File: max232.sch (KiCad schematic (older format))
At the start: 10 parts, among them J1 DB9, J2 DB9, P1 CONN_4, P2 CONN_4, U1 MAX232

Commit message: Version for iStudio.
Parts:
- removed J2: DB9, symbol DB9
- removed P1, P2: CONN_4, symbol CONN_4
- added P1: CONN_6, symbol CONN_6
- added P2, P3, P4, P5: CONN_1, symbol CONN_1
- added Q1, Q2: MOSFET_N, symbol MOSFET_N
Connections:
- net labels added: RD, RD_, TD, TD_
- wire segments 47 -> 59
- no-connect marks 12 -> 4

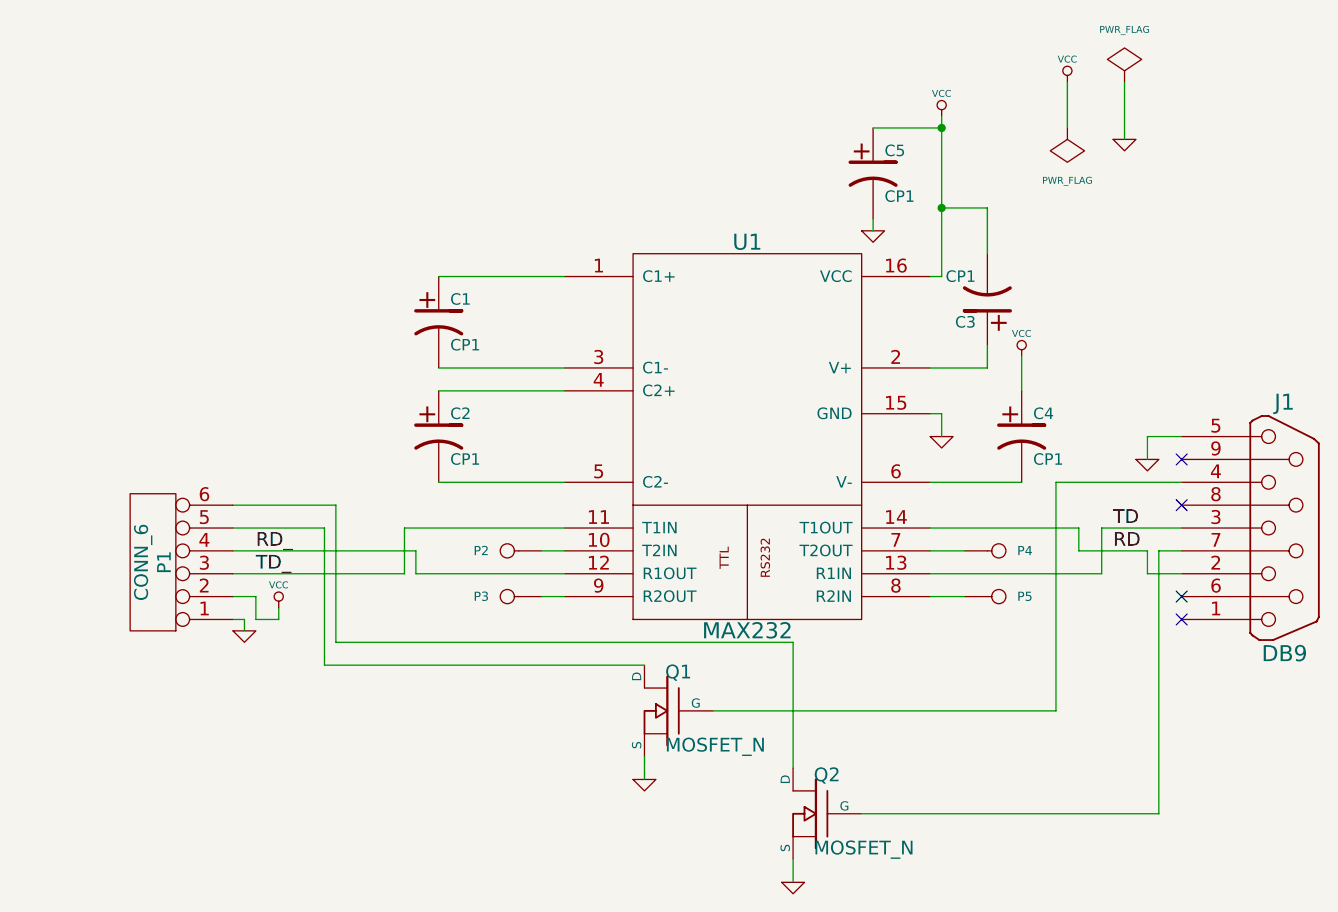
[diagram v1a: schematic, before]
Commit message: Fixed schemantick.
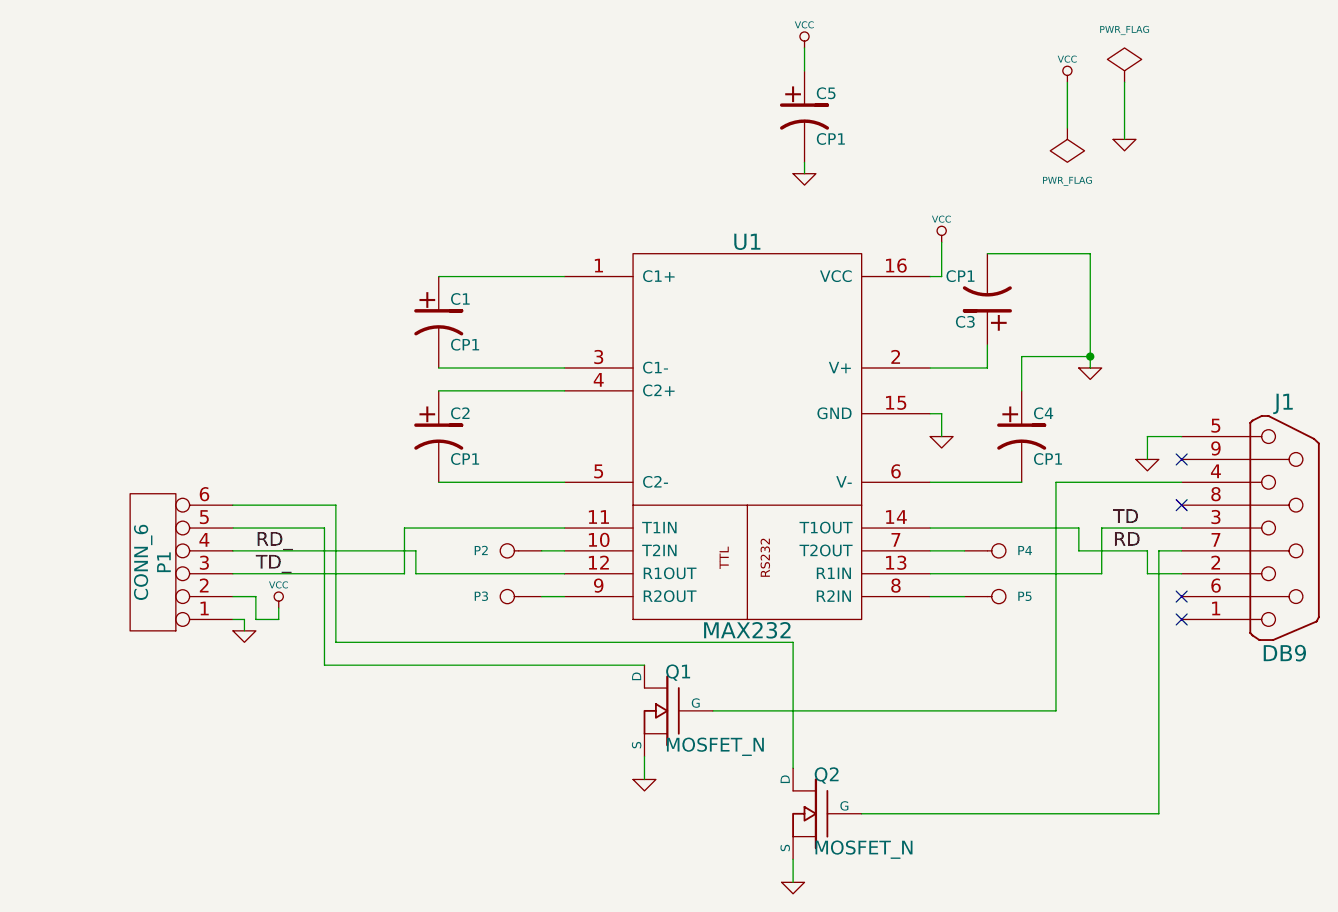
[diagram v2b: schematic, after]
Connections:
- net GND: now also C3.2, C4.1
- net VCC: no longer C3.2, C4.1
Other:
- moved on the sheet: C5
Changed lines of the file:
@@
-EESchema Schematic File Version 2  date Чт. 15 авг. 2013 22:17:01
+EESchema Schematic File Version 2  date Чт 05 сен 2013 11:55:04
 LIBS:power
 LIBS:device
@@
 Sheet 1 1
 Title ""
-Date "15 aug 2013"
+Date "5 sep 2013"
 Rev ""
 Comp ""
@@
 $EndDescr
 Wire Wire Line
-	2450 4300 3250 4300
-Wire Wire Line
-	3250 4300 3250 4400
-Wire Wire Line
-	3250 4400 3900 4400
+	5550 2950 5550 3100
+Wire Wire Line
+	6200 3500 6200 3000
+Wire Wire Line
+	6200 3000 5750 3000
+Wire Wire Line
+	2450 4400 3200 4400
+Wire Wire Line
+	3200 4400 3200 4200
+Wire Wire Line
+	3800 4300 3900 4300
+Wire Wire Line
+	5650 4500 5500 4500
+Wire Wire Line
+	6600 4300 6500 4300
+Wire Wire Line
+	6500 4300 6500 5450
+Wire Wire Line
+	6500 5450 5200 5450
+Wire Wire Line
+	2450 4100 2900 4100
+Wire Wire Line
+	2900 4100 2900 4700
+Wire Wire Line
+	2900 4700 4900 4700
+Wire Wire Line
+	4900 4700 4900 5250
+Wire Wire Line
+	4250 5200 4250 5300
+Wire Wire Line
+	2450 4500 2550 4500
+Wire Wire Line
+	2550 4500 2550 4600
+Wire Wire Line
+	2550 4600 2650 4600
+Wire Wire Line
+	2650 4600 2650 4550
+Wire Wire Line
+	6600 4400 6450 4400
+Wire Wire Line
+	6450 4400 6450 4300
+Wire Wire Line
+	6450 4300 6150 4300
+Wire Wire Line
+	6150 4300 6150 4200
+Wire Wire Line
+	6100 2450 6100 2250
+Wire Wire Line
+	5500 4000 5900 4000
+Wire Wire Line
+	5500 3500 5750 3500
+Wire Wire Line
+	5750 3500 5750 3400
+Wire Wire Line
+	5550 3100 5500 3100
+Wire Wire Line
+	3350 3600 3900 3600
+Wire Wire Line
+	3350 3100 3900 3100
+Wire Wire Line
+	3350 3500 3900 3500
+Wire Wire Line
+	3350 4000 3900 4000
+Wire Wire Line
+	4950 2600 4950 2650
+Wire Wire Line
+	5500 3700 5550 3700
+Wire Wire Line
+	5550 3700 5550 3800
+Wire Wire Line
+	5900 3600 5900 3450
+Wire Wire Line
+	6450 3900 6450 3800
+Wire Wire Line
+	6450 3800 6600 3800
+Wire Wire Line
+	6350 2250 6350 2500
+Wire Wire Line
+	5500 4400 6250 4400
+Wire Wire Line
+	6250 4400 6250 4200
+Wire Wire Line
+	6250 4200 6600 4200
+Wire Wire Line
+	6150 4200 5500 4200
+Wire Wire Line
+	2450 4600 2500 4600
+Wire Wire Line
+	2500 4600 2500 4650
+Wire Wire Line
+	4900 5650 4900 5750
+Wire Wire Line
+	4250 4800 2850 4800
+Wire Wire Line
+	2850 4800 2850 4200
+Wire Wire Line
+	2850 4200 2450 4200
+Wire Wire Line
+	4550 5000 6050 5000
+Wire Wire Line
+	6050 5000 6050 4000
+Wire Wire Line
+	6050 4000 6600 4000
+Wire Wire Line
+	5500 4300 5650 4300
+Wire Wire Line
+	3200 4200 3900 4200
 Wire Wire Line
 	3900 4500 3800 4500
 Wire Wire Line
-	3900 4200 3200 4200
-Wire Wire Line
-	5500 4300 5650 4300
-Wire Wire Line
-	6600 4000 6050 4000
-Wire Wire Line
-	6050 4000 6050 5000
-Wire Wire Line
-	6050 5000 4550 5000
-Wire Wire Line
-	2450 4200 2850 4200
-Wire Wire Line
-	2850 4200 2850 4800
-Wire Wire Line
-	2850 4800 4250 4800
-Wire Wire Line
-	4900 5650 4900 5750
-Wire Wire Line
-	2500 4650 2500 4600
-Wire Wire Line
-	2500 4600 2450 4600
-Wire Wire Line
-	5500 4200 6150 4200
-Wire Wire Line
-	6600 4200 6250 4200
-Wire Wire Line
-	6250 4200 6250 4400
-Wire Wire Line
-	6250 4400 5500 4400
-Wire Wire Line
-	6350 2250 6350 2500
-Connection ~ 5550 2450
-Wire Wire Line
-	5550 2400 5550 3100
-Wire Wire Line
-	6600 3800 6450 3800
-Wire Wire Line
-	6450 3800 6450 3900
-Wire Wire Line
-	5900 3600 5900 3450
-Wire Wire Line
-	5550 3800 5550 3700
-Wire Wire Line
-	5550 3700 5500 3700
-Connection ~ 5550 2800
-Wire Wire Line
-	5750 3000 5750 2800
-Wire Wire Line
-	5750 2800 5550 2800
-Wire Wire Line
-	5250 2850 5250 2900
-Wire Wire Line
-	3350 4000 3900 4000
-Wire Wire Line
-	3350 3500 3900 3500
-Wire Wire Line
-	3350 3100 3900 3100
-Wire Wire Line
-	3350 3600 3900 3600
-Wire Wire Line
-	5550 3100 5500 3100
-Wire Wire Line
-	5550 2450 5250 2450
-Wire Wire Line
-	5750 3400 5750 3500
-Wire Wire Line
-	5750 3500 5500 3500
-Wire Wire Line
-	5500 4000 5900 4000
-Wire Wire Line
-	6100 2450 6100 2250
-Wire Wire Line
-	6150 4200 6150 4300
-Wire Wire Line
-	6150 4300 6450 4300
-Wire Wire Line
-	6450 4300 6450 4400
-Wire Wire Line
-	6450 4400 6600 4400
-Wire Wire Line
-	2650 4550 2650 4600
-Wire Wire Line
-	2650 4600 2550 4600
-Wire Wire Line
-	2550 4600 2550 4500
-Wire Wire Line
-	2550 4500 2450 4500
-Wire Wire Line
-	4250 5200 4250 5300
-Wire Wire Line
-	4900 5250 4900 4700
-Wire Wire Line
-	4900 4700 2900 4700
-Wire Wire Line
-	2900 4700 2900 4100
-Wire Wire Line
-	2900 4100 2450 4100
-Wire Wire Line
-	5200 5450 6500 5450
-Wire Wire Line
-	6500 5450 6500 4300
-Wire Wire Line
-	6500 4300 6600 4300
-Wire Wire Line
-	5650 4500 5500 4500
-Wire Wire Line
-	3800 4300 3900 4300
-Wire Wire Line
-	3200 4200 3200 4400
-Wire Wire Line
-	3200 4400 2450 4400
+	3900 4400 3250 4400
+Wire Wire Line
+	3250 4400 3250 4300
+Wire Wire Line
+	3250 4300 2450 4300
+Wire Wire Line
+	5900 3450 6200 3450
+Connection ~ 6200 3450
+Wire Wire Line
+	4950 2100 4950 2200
+$Comp
+L VCC #PWR?
+U 1 1 522838C7
+P 5550 2950
+F 0 "#PWR?" H 5550 3050 30  0001 C CNN
+F 1 "VCC" H 5550 3050 30  0000 C CNN
+	1    5550 2950
+	1    0    0    -1
+$EndComp
+$Comp
+L GND #PWR?
+U 1 1 52283890
+P 6200 3500
+F 0 "#PWR?" H 6200 3500 30  0001 C CNN
+F 1 "GND" H 6200 3430 30  0001 C CNN
+	1    6200 3500
+	1    0    0    -1
+$EndComp
 $Comp
 L CONN_1 P2
@@
 $EndComp
 $Comp
-L VCC #PWR010
-U 1 1 4FB2957E
-P 5900 3450
-F 0 "#PWR010" H 5900 3550 30  0001 C CNN
-F 1 "VCC" H 5900 3550 30  0000 C CNN
-	1    5900 3450
-	1    0    0    -1
-$EndComp
-$Comp
 L CP1 C4
 U 1 1 4FB29575
@@
 L GND #PWR012
 U 1 1 4FB29531
-P 5250 2900
-F 0 "#PWR012" H 5250 2900 30  0001 C CNN
-F 1 "GND" H 5250 2830 30  0001 C CNN
-	1    5250 2900
+P 4950 2650
+F 0 "#PWR012" H 4950 2650 30  0001 C CNN
+F 1 "GND" H 4950 2580 30  0001 C CNN
+	1    4950 2650
 	1    0    0    -1
 $EndComp
@@
 L CP1 C5
 U 1 1 4FB2951F
-P 5250 2650
-F 0 "C5" H 5300 2750 50  0000 L CNN
-F 1 "CP1" H 5300 2550 50  0000 L CNN
-	1    5250 2650
+P 4950 2400
+F 0 "C5" H 5000 2500 50  0000 L CNN
+F 1 "CP1" H 5000 2300 50  0000 L CNN
+	1    4950 2400
 	1    0    0    -1
 $EndComp
@@
 L VCC #PWR013
 U 1 1 4FB294D8
-P 5550 2400
-F 0 "#PWR013" H 5550 2500 30  0001 C CNN
-F 1 "VCC" H 5550 2500 30  0000 C CNN
-	1    5550 2400
-	1    0    0    -1
-$EndComp
+P 4950 2100
+F 0 "#PWR013" H 4950 2200 30  0001 C CNN
+F 1 "VCC" H 4950 2200 30  0000 C CNN
+	1    4950 2100
+	1    0    0    -1
+$EndComp
